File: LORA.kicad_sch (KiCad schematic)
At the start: 2 parts, among them U17 RF_Module_Ai-Thinker-Ra-02

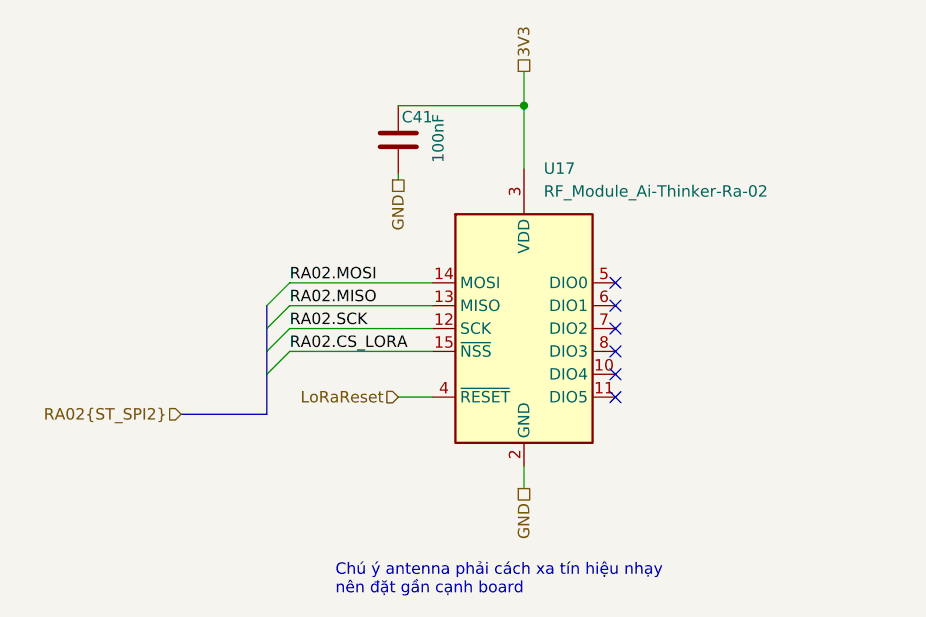
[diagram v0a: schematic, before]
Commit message: Add README, Lora received interrupt pin
Change LED pin from PB0 to PC13, PCF8563_CLKOUT to PC14
PB0 add Lora received interrupt pin
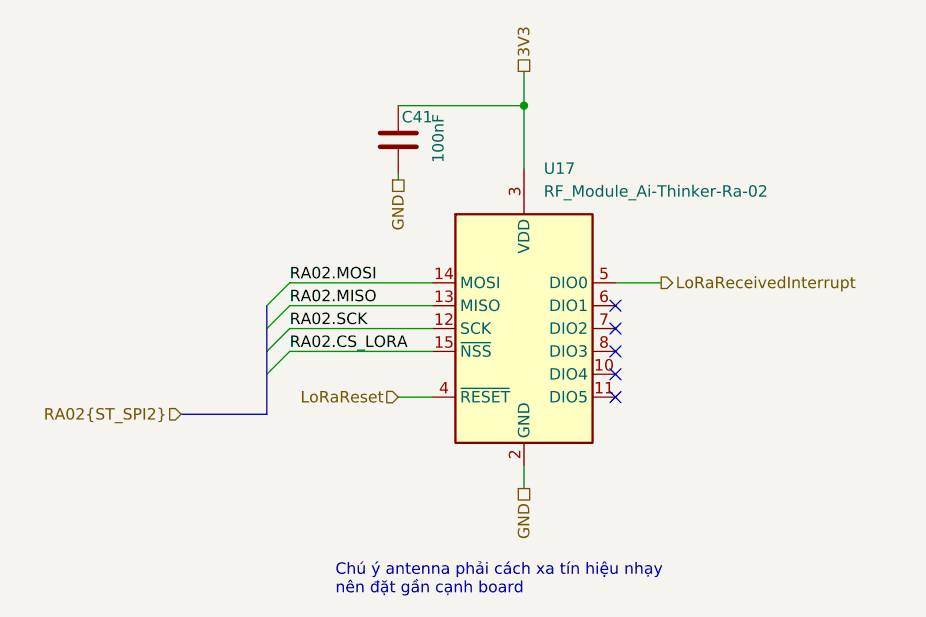
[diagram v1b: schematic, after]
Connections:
- net LoRaReceivedInterrupt: now reaches U17.5 (DIO0)
- no-connect marks 6 -> 5
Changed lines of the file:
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@@
 		(at 136.525 78.74)
 	)
-	(no_connect
-		(at 136.525 73.66)
-	)
 	(bus_entry
 		(at 100.33 76.2)
@@
 		(pts
 			(xy 112.395 62.23) (xy 112.395 61.595)
+		)
+		(stroke
+			(width 0)
+			(type default)
+		)
+	)
+	(wire
+		(pts
+			(xy 141.605 73.66) (xy 136.525 73.66)
 		)
 		(stroke
@@
 		(fields_autoplaced yes)
 		(effects
+			(font
+				(size 1.27 1.27)
+			)
+			(justify left)
+		)
+	)
+	(hierarchical_label "LoRaReceivedInterrupt"
+		(shape output)
+		(at 141.605 73.66 0)
+		(fields_autoplaced yes)
+		(effects
